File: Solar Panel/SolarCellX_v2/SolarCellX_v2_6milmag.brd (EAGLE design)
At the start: 100 x 82 mm, 16 parts

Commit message: Reviewed solar panel board
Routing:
- net V_SOLAR: track 118.6 -> 107.2 mm

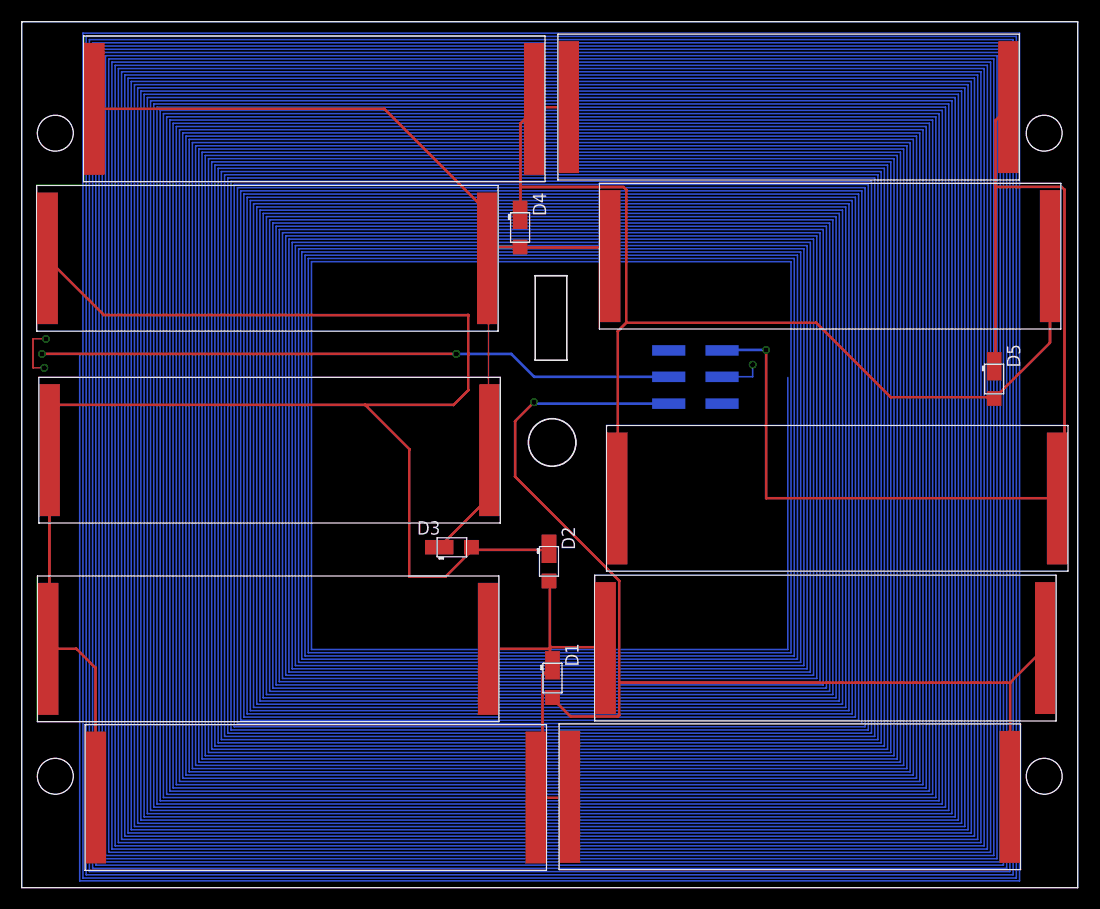
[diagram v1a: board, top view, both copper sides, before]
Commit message: Reviewed solar panel board - DRC
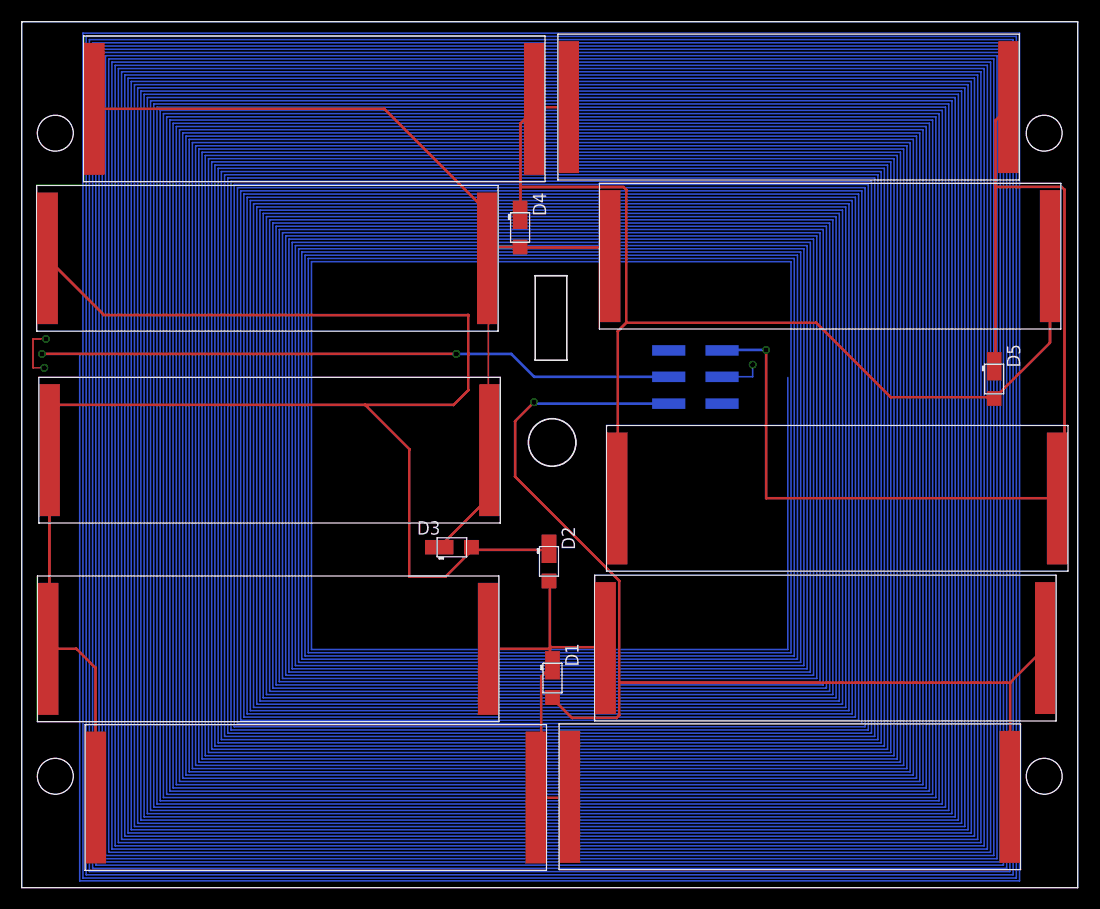
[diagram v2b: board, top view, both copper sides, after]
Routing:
- net N$3: track 153.6 -> 165.5 mm
- net N$5: track 82.4 -> 89.5 mm

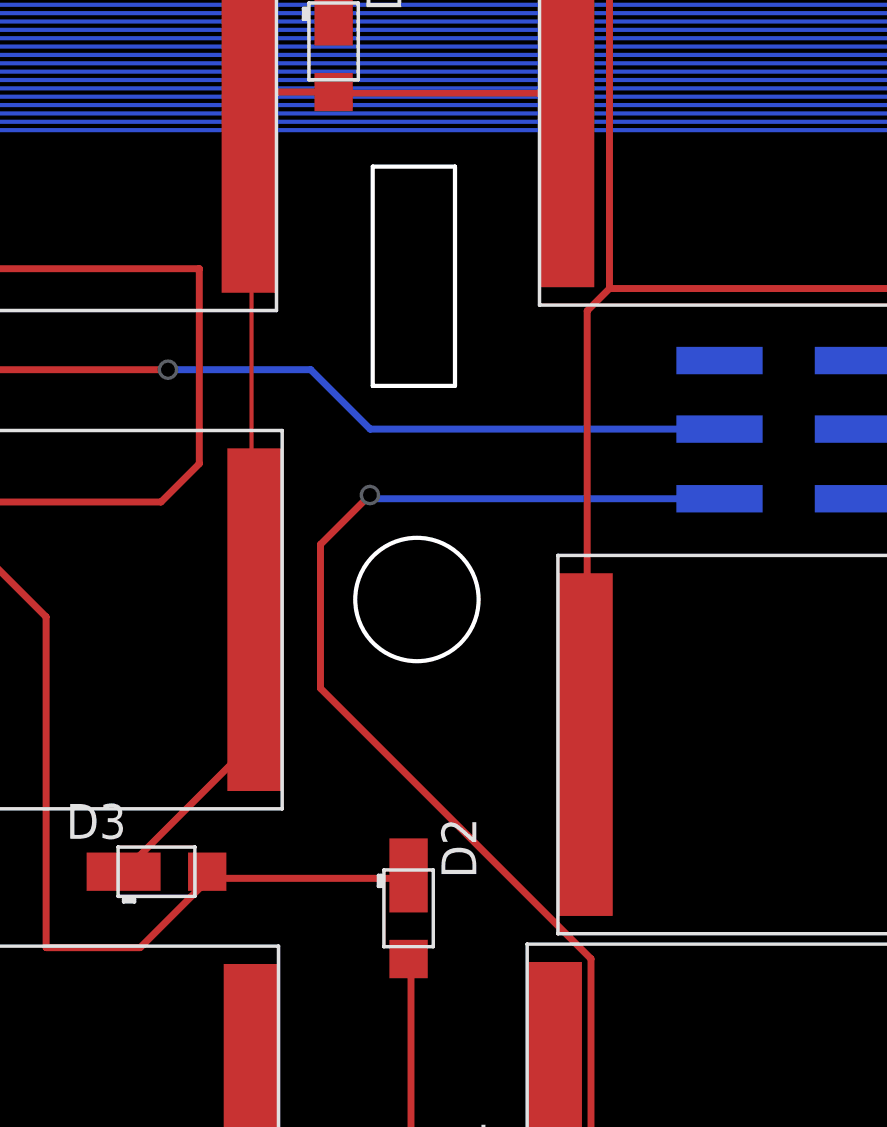
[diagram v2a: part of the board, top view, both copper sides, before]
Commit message: Changed the Connector cutout profile to give some wiggle room for tolerances
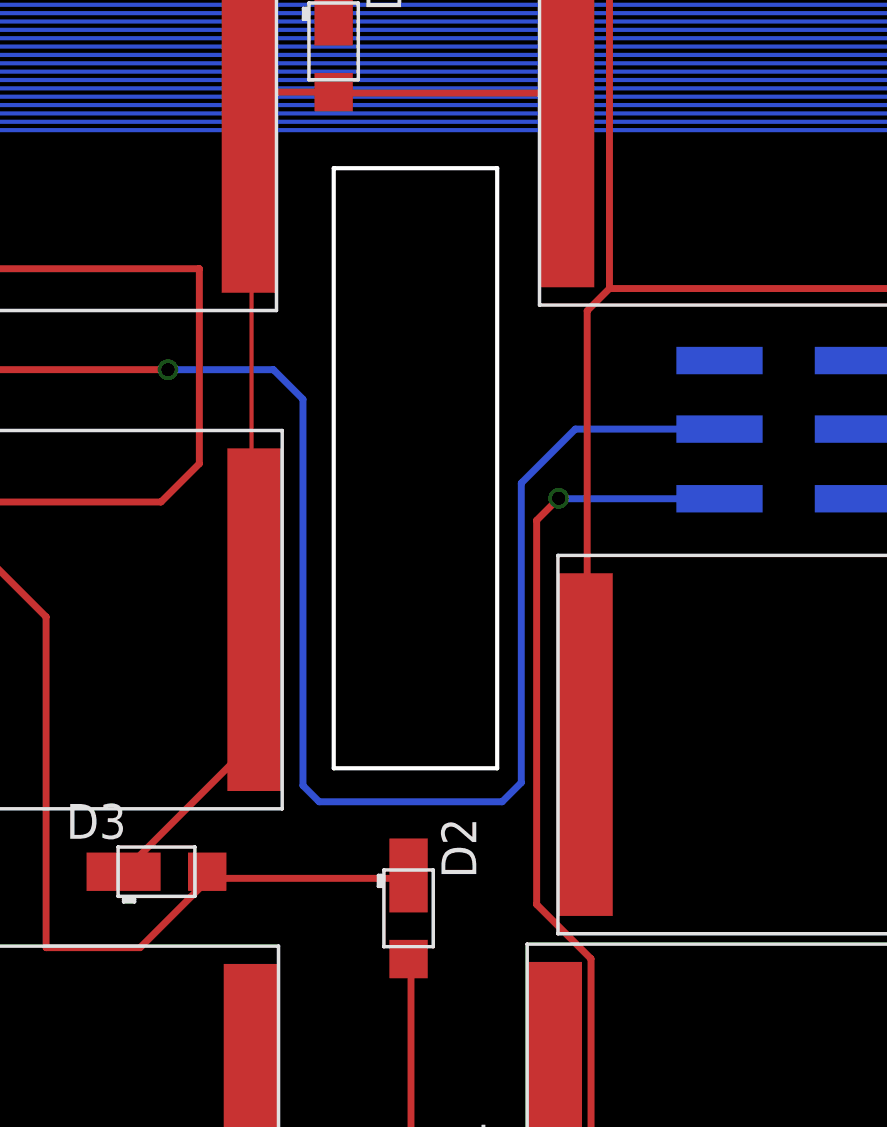
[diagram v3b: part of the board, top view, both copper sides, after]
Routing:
- net N$1: track 54672.2 -> 54698.2 mm
- net GND: track 107.1 -> 96.3 mm
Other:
- outline, holes or cut-outs redrawn
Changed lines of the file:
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@@
 <wire x1="100" y1="82" x2="100" y2="0" width="0.127" layer="20"/>
 <wire x1="100" y1="0" x2="0" y2="0" width="0.127" layer="20"/>
-<wire x1="48.617" y1="57.954" x2="51.617" y2="57.954" width="0.1524" layer="20"/>
-<wire x1="51.617" y1="57.954" x2="51.617" y2="49.954" width="0.1524" layer="20"/>
-<wire x1="51.617" y1="49.954" x2="48.617" y2="49.954" width="0.1524" layer="20"/>
-<wire x1="48.617" y1="49.954" x2="48.617" y2="57.954" width="0.1524" layer="20"/>
-<circle x="50.228" y="42.163" radius="2.25" width="0.1524" layer="20"/>
+<wire x1="47.1946" y1="57.895578125" x2="53.1562375" y2="57.895578125" width="0.1524" layer="20"/>
+<wire x1="53.1562375" y1="57.895578125" x2="53.1562375" y2="36.006859375" width="0.1524" layer="20"/>
+<wire x1="53.1562375" y1="36.006859375" x2="47.1946" y2="36.006859375" width="0.1524" layer="20"/>
+<wire x1="47.1946" y1="36.006859375" x2="47.1946" y2="57.895578125" width="0.1524" layer="20"/>
 </plain>
 <attributes>
@@
 <contactref element="D1" pad="POS"/>
 <contactref element="U$1" pad="P$1"/>
-<wire x1="61.265" y1="45.839" x2="48.514" y2="45.839" width="0.254" layer="16"/>
-<wire x1="48.514" y1="45.839" x2="48.514" y2="45.974" width="0.254" layer="16"/>
-<via x="48.514" y="45.974" extent="1-16" drill="0.5"/>
-<wire x1="48.514" y1="45.974" x2="46.7106" y2="44.1706" width="0.254" layer="1"/>
-<wire x1="46.7106" y1="44.1706" x2="46.7106" y2="38.9255" width="0.254" layer="1"/>
-<wire x1="56.5785" y1="29.0576" x2="46.7106" y2="38.9255" width="0.254" layer="1"/>
+<wire x1="61.265" y1="45.839" x2="55.399940625" y2="45.839" width="0.254" layer="16"/>
+<wire x1="55.399940625" y1="45.839" x2="55.399940625" y2="45.85461875" width="0.254" layer="16"/>
+<via x="55.399940625" y="45.85461875" extent="1-16" drill="0.5"/>
+<wire x1="55.399940625" y1="45.85461875" x2="54.5947625" y2="45.049440625" width="0.254" layer="1"/>
+<wire x1="54.5947625" y1="45.049440625" x2="54.5947625" y2="31.0413375" width="0.254" layer="1"/>
+<wire x1="56.5785" y1="29.0576" x2="54.5947625" y2="31.0413375" width="0.254" layer="1"/>
 <wire x1="56.5785" y1="16.3449" x2="56.5785" y2="19.4183" width="0.254" layer="1"/>
 <wire x1="56.5785" y1="19.4183" x2="56.5785" y2="29.0576" width="0.254" layer="1"/>
@@
 <contactref element="U$1" pad="P$3"/>
 <wire x1="61.265" y1="48.379" x2="61.13" y2="48.514" width="0.254" layer="16"/>
-<wire x1="61.265" y1="48.379" x2="48.522" y2="48.379" width="0.254" layer="16"/>
-<wire x1="46.355" y1="50.546" x2="41.148" y2="50.546" width="0.254" layer="16"/>
-<wire x1="48.522" y1="48.379" x2="46.355" y2="50.546" width="0.254" layer="16"/>
+<wire x1="61.265" y1="48.379" x2="60.487759375" y2="48.379" width="0.254" layer="16"/>
+<wire x1="60.487759375" y1="48.379" x2="60.416640625" y2="48.30788125" width="0.254" layer="16"/>
+<wire x1="41.148" y1="50.546" x2="44.9935625" y2="50.546" width="0.254" layer="16"/>
 <via x="41.148" y="50.546" extent="1-16" drill="0.5"/>
 <wire x1="41.148" y1="50.546" x2="1.905" y2="50.546" width="0.254" layer="1"/>
@@
 <wire x1="72.8472" y1="59.2836" x2="72.8472" y2="22.2504" width="0.1524" layer="2"/>
 <wire x1="27.432" y1="59.2836" x2="72.8472" y2="59.2836" width="0.1524" layer="2"/>
+<wire x1="46.071915625" y1="49.467646875" x2="46.071915625" y2="35.37625625" width="0.254" layer="16"/>
+<wire x1="46.071915625" y1="35.37625625" x2="46.66305625" y2="34.785115625" width="0.254" layer="16"/>
+<wire x1="46.66305625" y1="34.785115625" x2="53.337278125" y2="34.785115625" width="0.254" layer="16"/>
+<wire x1="53.337278125" y1="34.785115625" x2="54.0350875" y2="35.482925" width="0.254" layer="16"/>
+<wire x1="54.0350875" y1="35.482925" x2="54.0350875" y2="46.40746875" width="0.254" layer="16"/>
+<wire x1="56.00661875" y1="48.379" x2="60.487759375" y2="48.379" width="0.254" layer="16"/>
+<wire x1="44.9935625" y1="50.546" x2="46.071915625" y2="49.467646875" width="0.254" layer="16"/>
+<wire x1="54.0350875" y1="46.40746875" x2="56.00661875" y2="48.379" width="0.254" layer="16"/>
 <wire x1="72.8472" y1="59.2836" x2="72.8472" y2="59.2836" width="0" layer="19" extent="15-16"/>
 </signal>

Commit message: Finalized board and gerber files finished
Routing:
- net N$1: track 54698.2 -> 54699.3 mm, vias 5 -> 6
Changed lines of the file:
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@@
 <setting verticaltext="up"/>
 </settings>
-<grid distance="0.1" unitdist="mil" unit="mil" style="lines" multiple="1" display="yes" altdistance="1" altunitdist="mm" altunit="mm"/>
+<grid distance="6" unitdist="mil" unit="mil" style="lines" multiple="1" display="yes" altdistance="1" altunitdist="mm" altunit="mm"/>
 <layers>
 <layer number="1" name="Top" color="4" fill="1" visible="yes" active="yes"/>
@@
 <layer number="15" name="Route15" color="23" fill="1" visible="yes" active="yes"/>
 <layer number="16" name="Bottom" color="1" fill="1" visible="yes" active="yes"/>
-<layer number="17" name="Pads" color="2" fill="1" visible="yes" active="yes"/>
+<layer number="17" name="Pads" color="2" fill="1" visible="no" active="yes"/>
 <layer number="18" name="Vias" color="2" fill="1" visible="yes" active="yes"/>
 <layer number="19" name="Unrouted" color="6" fill="1" visible="yes" active="yes"/>
-<layer number="20" name="Dimension" color="24" fill="1" visible="yes" active="yes"/>
-<layer number="21" name="tPlace" color="7" fill="1" visible="yes" active="yes"/>
-<layer number="22" name="bPlace" color="7" fill="1" visible="yes" active="yes"/>
-<layer number="23" name="tOrigins" color="15" fill="1" visible="yes" active="yes"/>
-<layer number="24" name="bOrigins" color="15" fill="1" visible="yes" active="yes"/>
+<layer number="20" name="Dimension" color="24" fill="1" visible="no" active="yes"/>
+<layer number="21" name="tPlace" color="7" fill="1" visible="no" active="yes"/>
+<layer number="22" name="bPlace" color="7" fill="1" visible="no" active="yes"/>
+<layer number="23" name="tOrigins" color="15" fill="1" visible="no" active="yes"/>
+<layer number="24" name="bOrigins" color="15" fill="1" visible="no" active="yes"/>
 <layer number="25" name="tNames" color="7" fill="1" visible="no" active="yes"/>
 <layer number="26" name="bNames" color="7" fill="1" visible="no" active="yes"/>
@@
 <wire x1="72.8472" y1="22.2504" x2="72.8472" y2="59.2836" width="0.1524" layer="16"/>
 <wire x1="72.8472" y1="59.2836" x2="27.432" y2="59.2836" width="0.1524" layer="16"/>
-<wire x1="27.432" y1="22.5552" x2="27.432" y2="59.2836" width="0.1524" layer="16"/>
-<wire x1="72.5424" y1="22.5552" x2="72.5424" y2="48.3108" width="0.1524" layer="16"/>
+<wire x1="27.432" y1="59.2836" x2="27.432" y2="22.5552" width="0.1524" layer="16"/>
 <wire x1="2.1336" y1="49.2252" x2="1.9812" y2="49.2252" width="0.1524" layer="15"/>
 <via x="2.1336" y="49.2252" extent="1-16" drill="0.5"/>
@@
 <wire x1="72.5424" y1="53.0264" x2="58.2168" y2="53.0264" width="0.1524" layer="2"/>
 <wire x1="72.5424" y1="22.5552" x2="72.5424" y2="53.0264" width="0.1524" layer="2"/>
-<wire x1="72.5424" y1="22.5552" x2="27.432" y2="22.5552" width="0.1524" layer="16"/>
 <wire x1="27.7368" y1="58.9788" x2="72.5424" y2="58.9788" width="0.1524" layer="15"/>
 <wire x1="27.7368" y1="22.5552" x2="27.7368" y2="58.9788" width="0.1524" layer="15"/>
@@
 <wire x1="44.9935625" y1="50.546" x2="46.071915625" y2="49.467646875" width="0.254" layer="16"/>
 <wire x1="54.0350875" y1="46.40746875" x2="56.00661875" y2="48.379" width="0.254" layer="16"/>
-<wire x1="72.8472" y1="59.2836" x2="72.8472" y2="59.2836" width="0" layer="19" extent="15-16"/>
+<wire x1="27.432" y1="22.5552" x2="72.5424" y2="22.5552" width="0.1524" layer="16"/>
+<wire x1="72.5424" y1="47.5167" x2="71.628" y2="47.5167" width="0.1524" layer="15"/>
+<wire x1="71.628" y1="47.5167" x2="71.628" y2="47.5488" width="0.1524" layer="15"/>
+<via x="71.628" y="47.5488" extent="1-16" drill="0.35"/>
+<wire x1="72.5424" y1="47.5488" x2="71.628" y2="47.5488" width="0.1524" layer="16"/>
+<wire x1="72.5424" y1="22.5552" x2="72.5424" y2="47.5488" width="0.1524" layer="16"/>
 </signal>
 </signals>
@@
 <mfgpreviewcolor name="substratecolor" color="0xFF786E46"/>
 </mfgpreviewcolors>
+<errors>
+</errors>
 </board>
 </drawing>
